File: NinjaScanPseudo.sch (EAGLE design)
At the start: 60 parts, among them CON2 ZX62-B-5PA(11), CON3 JST_SH-12SM, IC1 LTC3550EDHC, IC2 MPU-6000, IC4 MAG3110FCR, J1 JUMPER1608, U1 DM3AT-SF-PEJM5, U2 H.FL, U3 NEO-6T, U4 MS5611-01BA01

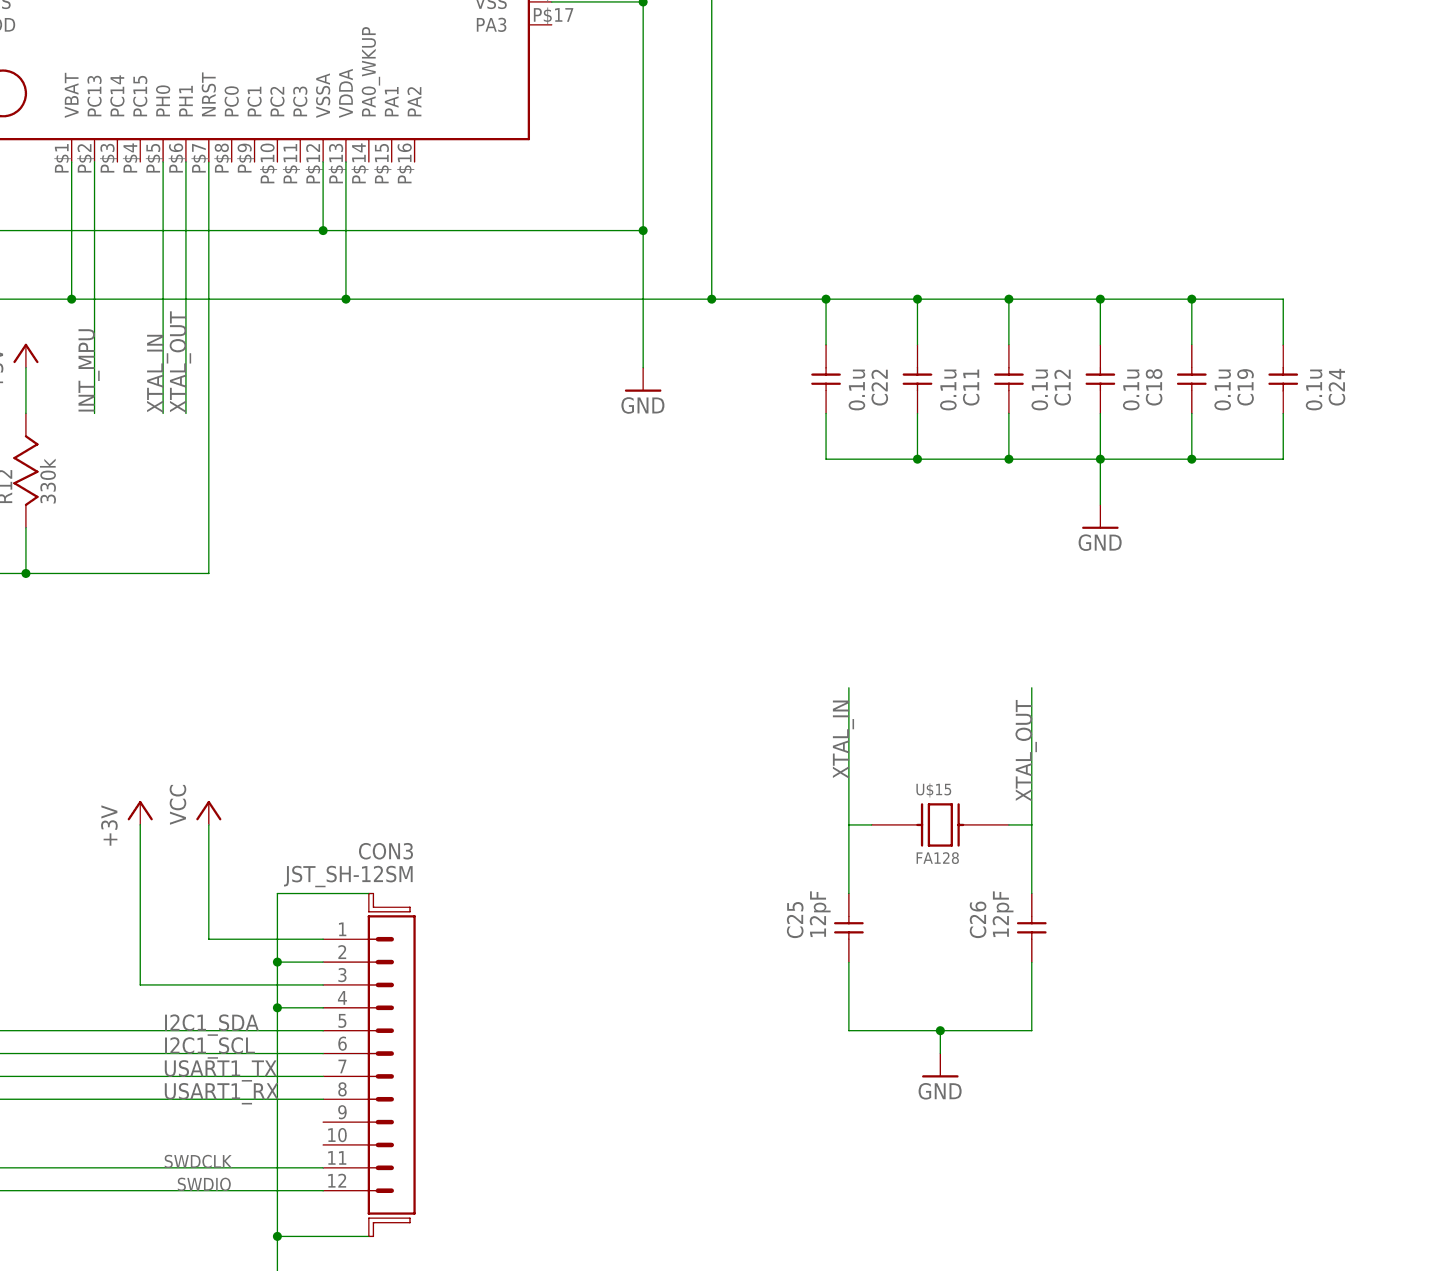
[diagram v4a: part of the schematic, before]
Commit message: CMOS Xtal added
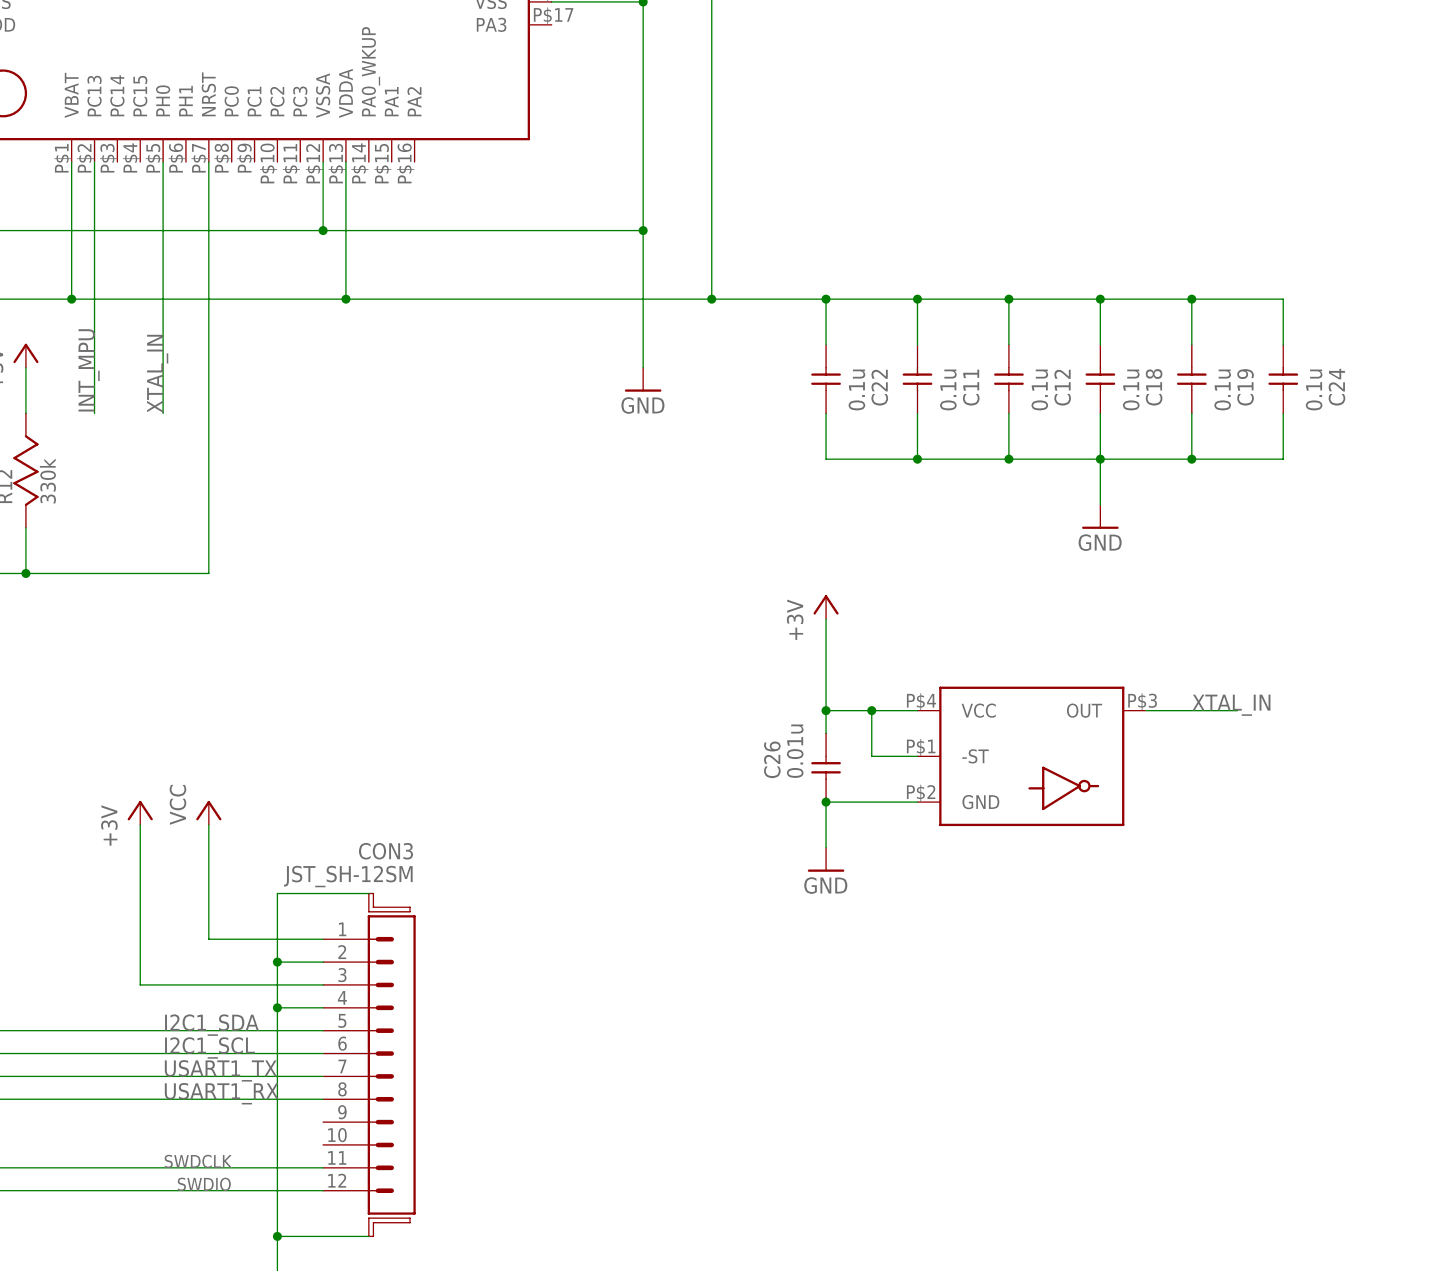
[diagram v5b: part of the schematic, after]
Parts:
- removed C25: 12pF, additional:C1005
- C26: value 12pF -> 0.01u
- U$15: value FA128 -> SG-210; device mami_pero:FA128 -> mami_pero:SG-210
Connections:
- removed net XTAL_OUT: C26.2, U$15.P$2, U$6.PH1
- net +3V: now also C26.2, U$15.-ST, U$15.VCC
- net GND: now also U$15.GND; no longer C25.1
- net XTAL_IN: now also U$15.OUT; no longer C25.2, U$15.P$1
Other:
- moved on the sheet: C26
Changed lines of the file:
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@@
 <part name="C19" library="additional" deviceset="C" device="1005" value="0.1u"/>
 <part name="C24" library="additional" deviceset="C" device="1005" value="0.1u"/>
-<part name="U$15" library="mami_pero" deviceset="FA128" device=""/>
-<part name="C25" library="additional" deviceset="C" device="1005" value="12pF"/>
-<part name="C26" library="additional" deviceset="C" device="1005" value="12pF"/>
 <part name="GND11" library="supply1" deviceset="GND" device=""/>
+<part name="U$15" library="mami_pero" deviceset="SG-210" device=""/>
+<part name="U$17" library="supply1" deviceset="+3V" device=""/>
+<part name="C26" library="additional" deviceset="C" device="1005" value="0.01u"/>
 </parts>
 <sheets>
@@
 <instance part="C19" gate="G$1" x="45.72" y="-121.92" rot="R270"/>
 <instance part="C24" gate="G$1" x="55.88" y="-121.92" rot="R270"/>
-<instance part="U$15" gate="G$1" x="15.24" y="-170.18"/>
-<instance part="C25" gate="G$1" x="7.62" y="-180.34" rot="R90"/>
-<instance part="C26" gate="G$1" x="27.94" y="-180.34" rot="R90"/>
-<instance part="GND11" gate="1" x="17.78" y="-198.12"/>
+<instance part="GND11" gate="1" x="5.08" y="-175.26"/>
+<instance part="U$15" gate="G$1" x="17.78" y="-167.64"/>
+<instance part="U$17" gate="G$1" x="5.08" y="-144.78"/>
+<instance part="C26" gate="G$1" x="5.08" y="-162.56" rot="R90"/>
 </instances>
 <busses>
@@
 </segment>
 <segment>
-<pinref part="C25" gate="G$1" pin="1"/>
-<wire x1="7.62" y1="-185.42" x2="7.62" y2="-193.04" width="0.1524" layer="91"/>
+<pinref part="GND11" gate="1" pin="GND"/>
+<wire x1="5.08" y1="-172.72" x2="5.08" y2="-167.64" width="0.1524" layer="91"/>
+<pinref part="U$15" gate="G$1" pin="GND"/>
+<wire x1="15.24" y1="-167.64" x2="5.08" y2="-167.64" width="0.1524" layer="91"/>
 <pinref part="C26" gate="G$1" pin="1"/>
-<wire x1="7.62" y1="-193.04" x2="17.78" y2="-193.04" width="0.1524" layer="91"/>
-<wire x1="17.78" y1="-193.04" x2="27.94" y2="-193.04" width="0.1524" layer="91"/>
-<wire x1="27.94" y1="-193.04" x2="27.94" y2="-185.42" width="0.1524" layer="91"/>
-<pinref part="GND11" gate="1" pin="GND"/>
-<wire x1="17.78" y1="-195.58" x2="17.78" y2="-193.04" width="0.1524" layer="91"/>
-<junction x="17.78" y="-193.04"/>
+<junction x="5.08" y="-167.64"/>
 </segment>
 </net>
@@
 <pinref part="R12" gate="G$1" pin="2"/>
 </segment>
+<segment>
+<pinref part="U$15" gate="G$1" pin="VCC"/>
+<wire x1="15.24" y1="-157.48" x2="10.16" y2="-157.48" width="0.1524" layer="91"/>
+<wire x1="10.16" y1="-157.48" x2="5.08" y2="-157.48" width="0.1524" layer="91"/>
+<wire x1="5.08" y1="-157.48" x2="5.08" y2="-160.02" width="0.1524" layer="91"/>
+<pinref part="U$15" gate="G$1" pin="-ST"/>
+<wire x1="15.24" y1="-162.56" x2="10.16" y2="-162.56" width="0.1524" layer="91"/>
+<wire x1="10.16" y1="-162.56" x2="10.16" y2="-157.48" width="0.1524" layer="91"/>
+<junction x="10.16" y="-157.48"/>
+<pinref part="U$17" gate="G$1" pin="+3V"/>
+<wire x1="5.08" y1="-157.48" x2="5.08" y2="-147.32" width="0.1524" layer="91"/>
+<junction x="5.08" y="-157.48"/>
+<pinref part="C26" gate="G$1" pin="2"/>
+</segment>
 </net>
 <net name="AGND" class="0">
@@
 </segment>
 <segment>
-<pinref part="U$15" gate="G$1" pin="P$1"/>
-<pinref part="C25" gate="G$1" pin="2"/>
-<wire x1="10.16" y1="-170.18" x2="7.62" y2="-170.18" width="0.1524" layer="91"/>
-<wire x1="7.62" y1="-170.18" x2="7.62" y2="-177.8" width="0.1524" layer="91"/>
-<wire x1="7.62" y1="-170.18" x2="7.62" y2="-154.94" width="0.1524" layer="91"/>
-<label x="7.62" y="-165.1" size="1.778" layer="95" rot="R90"/>
-</segment>
-</net>
-<net name="XTAL_OUT" class="0">
-<segment>
-<pinref part="U$6" gate="G$1" pin="PH1"/>
-<wire x1="-66.04" y1="-96.52" x2="-66.04" y2="-124.46" width="0.1524" layer="91"/>
-<label x="-66.04" y="-124.46" size="1.778" layer="95" rot="R90"/>
-</segment>
-<segment>
-<pinref part="U$15" gate="G$1" pin="P$2"/>
-<pinref part="C26" gate="G$1" pin="2"/>
-<wire x1="25.4" y1="-170.18" x2="27.94" y2="-170.18" width="0.1524" layer="91"/>
-<wire x1="27.94" y1="-170.18" x2="27.94" y2="-177.8" width="0.1524" layer="91"/>
-<wire x1="27.94" y1="-170.18" x2="27.94" y2="-154.94" width="0.1524" layer="91"/>
-<label x="27.94" y="-167.64" size="1.778" layer="95" rot="R90"/>
-</segment>
-</net>
+<pinref part="U$15" gate="G$1" pin="OUT"/>
+<wire x1="40.64" y1="-157.48" x2="50.8" y2="-157.48" width="0.1524" layer="91"/>
+<label x="45.72" y="-157.48" size="1.778" layer="95"/>
+</segment>
+</net>
